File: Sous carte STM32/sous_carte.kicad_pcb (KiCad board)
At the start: 2 copper layers, 9 parts, among them J1 RJ45, P1 CONN_25X2, P2 CONN_25X2, P3 CONN_10, P4 CONN_10, P5 CONN_25X2, P6 CONN_2, P7 CONN_2, P8 CONN_2

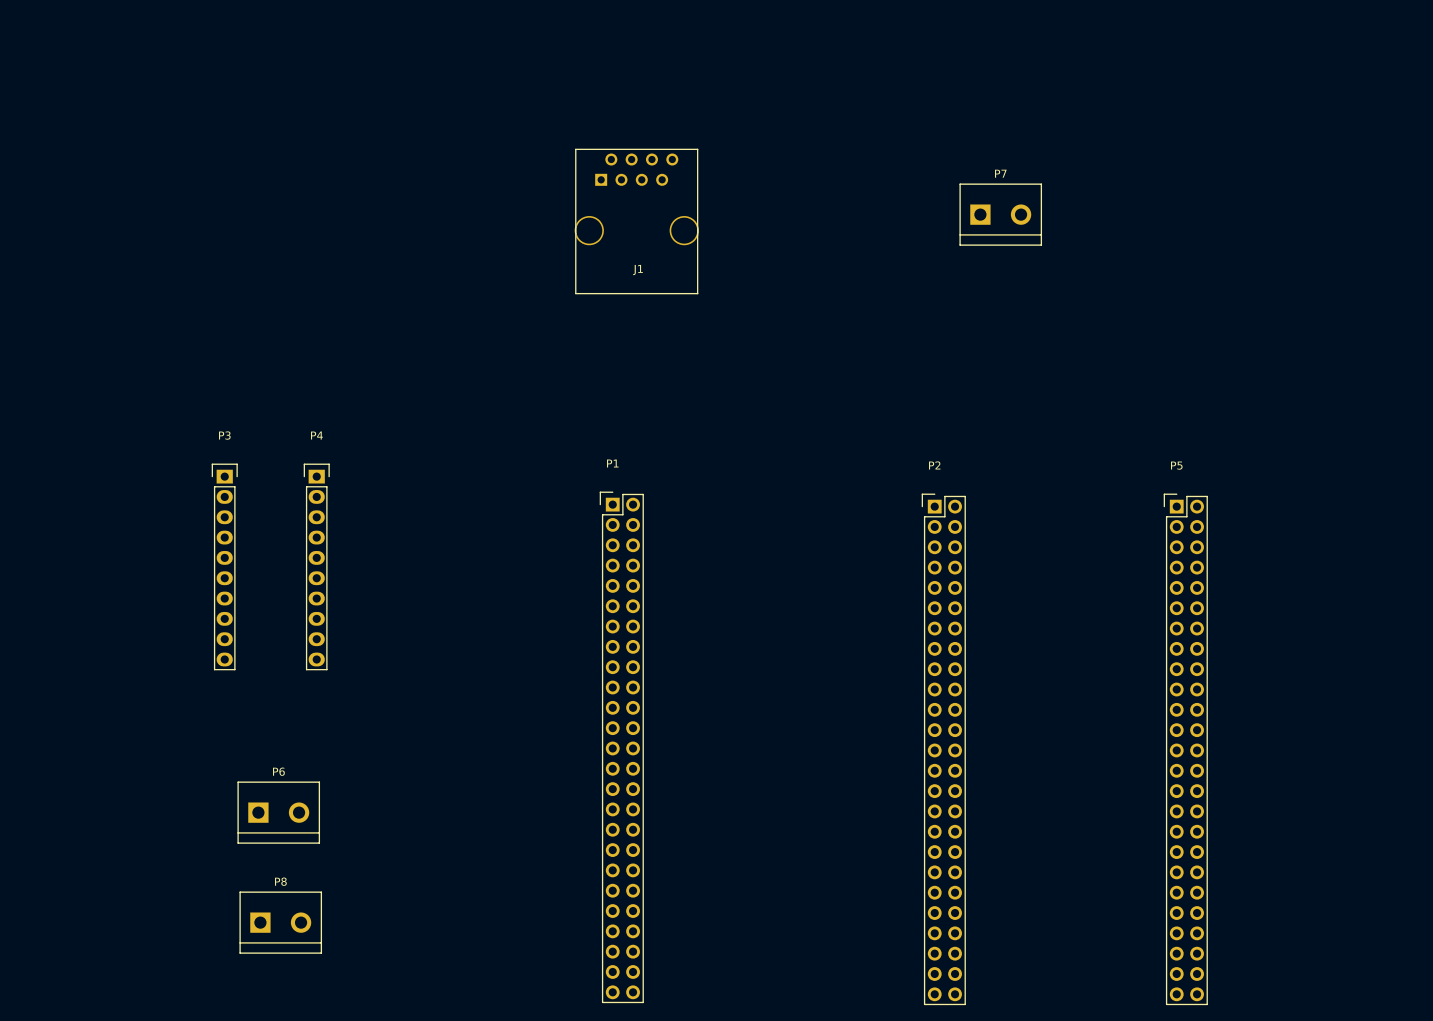
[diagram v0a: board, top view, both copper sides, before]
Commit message: fin schemas + début routage
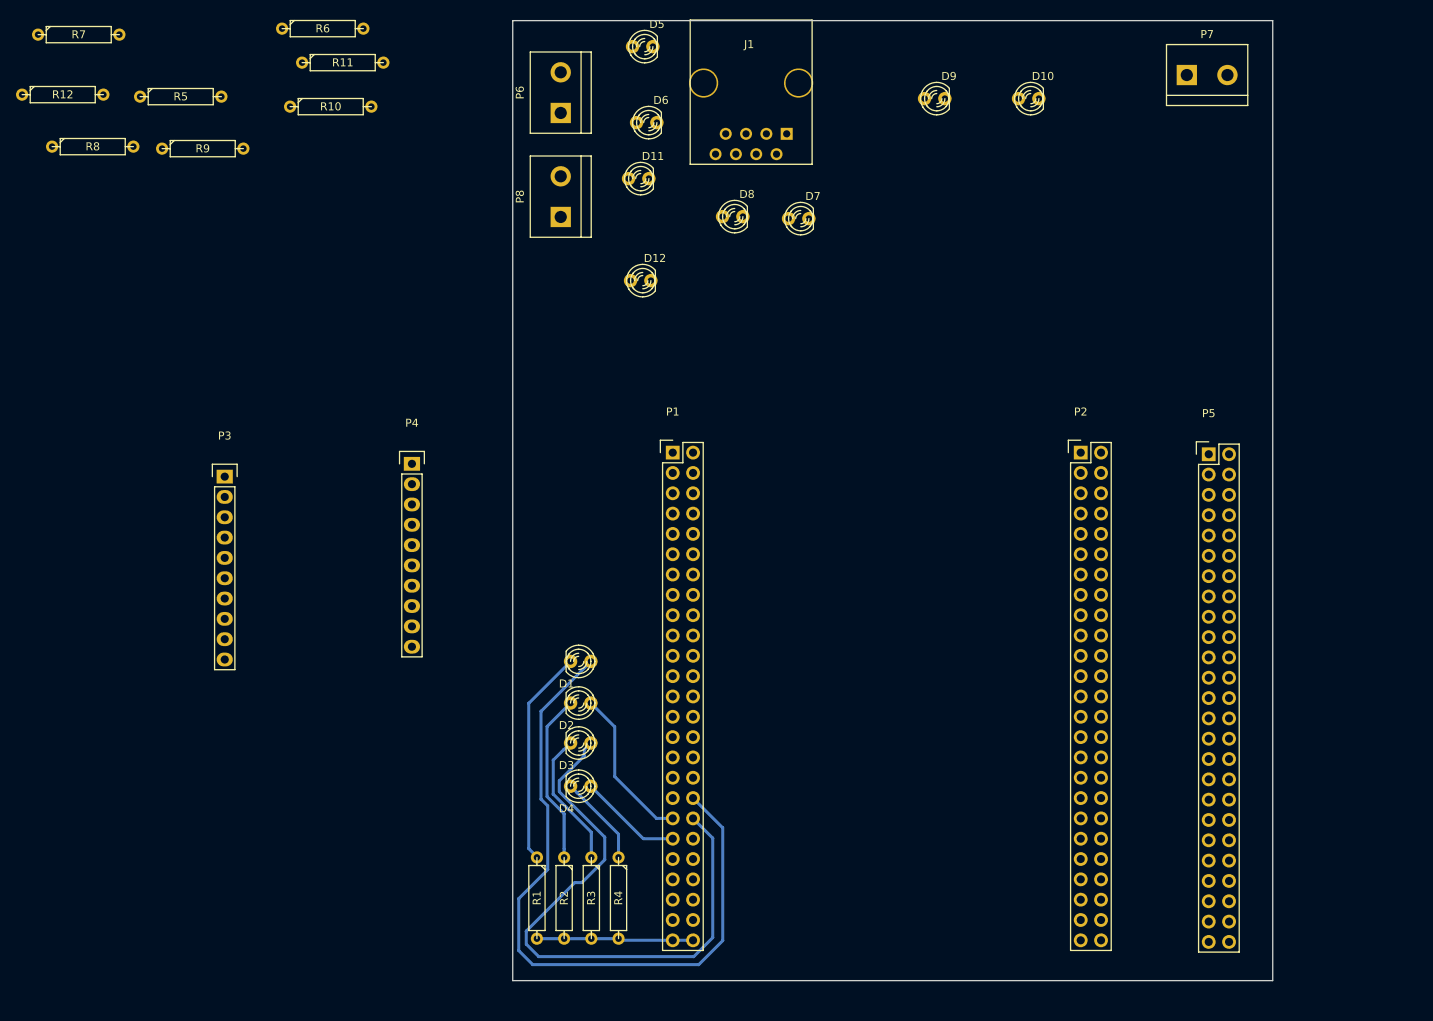
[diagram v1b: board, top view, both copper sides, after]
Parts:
- added D1: LED, LEDs:LED-3MM, F.Cu at (98.5, 126.1)
- added D10: LED, LEDs:LED-3MM, F.Cu at (154.5, 55.8)
- added D11: LED, LEDs:LED-3MM, F.Cu at (105.8, 65.8)
- added D12: LED, LEDs:LED-3MM, F.Cu at (106.0, 78.5)
- added D2: LED, LEDs:LED-3MM, F.Cu at (98.5, 131.3)
- added D3: LED, LEDs:LED-3MM, F.Cu at (98.5, 136.3)
- added D4: LED, LEDs:LED-3MM, F.Cu at (98.5, 141.7)
- added D5: LED, LEDs:LED-3MM, F.Cu at (106.2, 49.2)
- added D6: LED, LEDs:LED-3MM, F.Cu at (106.8, 58.8)
- added D7: LED, LEDs:LED-3MM, F.Cu at (125.8, 70.8)
- added D8: LED, LEDs:LED-3MM, F.Cu at (117.5, 70.5)
- added D9: LED, LEDs:LED-3MM, F.Cu at (142.8, 55.8)
- added R1: R, Discret:R4, F.Cu at (93.0, 155.7)
- added R10: R, Discret:R4, F.Cu at (67.2, 56.8)
- added R11: R, Discret:R4, F.Cu at (68.8, 51.2)
- added R12: R, Discret:R4, F.Cu at (33.8, 55.2)
- added R2: R, Discret:R4, F.Cu at (96.4, 155.7)
- added R3: R, Discret:R4, F.Cu at (99.8, 155.7)
- added R4: R, Discret:R4, F.Cu at (103.2, 155.7)
- added R5: R, Discret:R4, F.Cu at (48.5, 55.5)
- added R6: R, Discret:R4, F.Cu at (66.2, 47.0)
- added R7: R, Discret:R4, F.Cu at (35.8, 47.8)
- added R8: R, Discret:R4, F.Cu at (37.5, 61.8)
- added R9: R, Discret:R4, F.Cu at (51.2, 62.0)
- moved P8 97.3 mm to (96.0, 68.0), turned to 90 degrees
- moved P6 96.7 mm to (96.0, 55.0), turned to 90 degrees
- moved P7 31.1 mm to (176.8, 52.8)
- moved J1 23.3 mm to (119.8, 53.8), turned to 180 degrees
- moved P2 19.5 mm to (161.0, 100.0)
- moved P4 12.0 mm to (77.4, 101.4)
- moved P1 9.92 mm to (110.0, 100.0)
- moved P5 7.67 mm to (177.0, 100.2)
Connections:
- net +3.3V renamed 3V3
- net +5V renamed 5V
- net Net-(P1-Pad10) renamed C2
- net Net-(P1-Pad19) renamed C5
- net Net-(P1-Pad20) renamed C4
- net Net-(P1-Pad21) renamed B1
- net Net-(P1-Pad22) renamed B0
- net Net-(P1-Pad24) renamed B2
- net Net-(P1-Pad3) renamed VDD1
- net Net-(P1-Pad4) renamed VDD2
- net Net-(P1-Pad41) renamed D9
- net Net-(P1-Pad42) renamed D10
- net Net-(P1-Pad43) renamed D11
- net Net-(P1-Pad44) renamed D12
- net Net-(P1-Pad45) renamed D13
- net Net-(P1-Pad46) renamed D14
- net Net-(P1-Pad47) renamed D15
- net Net-(P1-Pad48) renamed NC
- net Net-(P1-Pad6) renamed NRST
- net Net-(P1-Pad7) renamed C1
- net Net-(P1-Pad8) renamed C0
- net Net-(P1-Pad9) renamed C3
- net Net-(P2-Pad10) renamed C15
- net Net-(P2-Pad12) renamed C13
- net Net-(P2-Pad15) renamed E2
- net Net-(P2-Pad16) renamed E3
- net Net-(P2-Pad17) renamed E0
- net Net-(P2-Pad18) renamed E1
- net Net-(P2-Pad21) renamed BOOT0
- net Net-(P2-Pad22) renamed VDD3
- net Net-(P2-Pad27) renamed D7
- net Net-(P2-Pad31) renamed D3
- net Net-(P2-Pad32) renamed D4
- net Net-(P2-Pad33) renamed D1
- net Net-(P2-Pad39) renamed A14
- net Net-(P2-Pad40) renamed A15
- net Net-(P2-Pad42) renamed A13
- net Net-(P2-Pad7) renamed H0
- net Net-(P2-Pad8) renamed H1
- net Net-(P2-Pad9) renamed C14
- P1 pad 11: UART4_RX -> A1
- P1 pad 12: UART4_TX -> A0
- P1 pad 13: UART2_RX -> A3
- P1 pad 14: UART2_TX -> A2
- P1 pad 15: Net-(P1-Pad15) -> A5
- P1 pad 16: Net-(P1-Pad16) -> A4
- P1 pad 17: Net-(P1-Pad17) -> A7
- P1 pad 18: Net-(P1-Pad18) -> A6
- P1 pad 25: Net-(P1-Pad25) -> E7
- P1 pad 26: Net-(P1-Pad26) -> E8
- P1 pad 27: Net-(P1-Pad27) -> E9
- P1 pad 28: Net-(P1-Pad28) -> E10
- P1 pad 29: Net-(P1-Pad29) -> E11
- P1 pad 30: Net-(P1-Pad30) -> E12
- P1 pad 31: Net-(P1-Pad31) -> E13
- P1 pad 32: Net-(P1-Pad32) -> E14
- P1 pad 33: Net-(P1-Pad33) -> E15
- P1 pad 34: Net-(P1-Pad34) -> B10
- P1 pad 35: Net-(P1-Pad35) -> B11
- P1 pad 36: Net-(P1-Pad36) -> B12
- P1 pad 37: Net-(P1-Pad37) -> B13
- P1 pad 38: Net-(P1-Pad38) -> B14
- P1 pad 39: Net-(P1-Pad39) -> B15
- P2 pad 11: Net-(P2-Pad11) -> E6
- P2 pad 13: Net-(P2-Pad13) -> E4
- P2 pad 14: Net-(P2-Pad14) -> E5
- P2 pad 19: Net-(P2-Pad19) -> B8
- P2 pad 20: Net-(P2-Pad20) -> B9
- P2 pad 23: Net-(P2-Pad23) -> B6
- P2 pad 24: Net-(P2-Pad24) -> B7
- P2 pad 25: Net-(P2-Pad25) -> B4
- P2 pad 26: Net-(P2-Pad26) -> B5
- P2 pad 28: Net-(P2-Pad28) -> B3
- P2 pad 29: Net-(P2-Pad29) -> UART2_TX
- P2 pad 30: Net-(P2-Pad30) -> D6
- P2 pad 34: Net-(P2-Pad34) -> D2
- P2 pad 35: Net-(P2-Pad35) -> C12
- P2 pad 36: Net-(P2-Pad36) -> C12
- P2 pad 37: Net-(P2-Pad37) -> C10
- P2 pad 38: Net-(P2-Pad38) -> UART4_RX
- P2 pad 41: Net-(P2-Pad41) -> A10
- P2 pad 43: Net-(P2-Pad43) -> A8
- P2 pad 44: Net-(P2-Pad44) -> A9
- P2 pad 45: Net-(P2-Pad45) -> C8
- P2 pad 46: Net-(P2-Pad46) -> C9
- P2 pad 47: UART6_TX -> C6
- P2 pad 48: UART6_RX -> C7
- P3 pad 2: UART2_RX -> UART4_RX
- P3 pad 3: UART2_TX -> C10
- P5 pad 11: Net-(P1-Pad16) -> A0
- P5 pad 13: Net-(P1-Pad17) -> A3
- P5 pad 14: Net-(P5-Pad14) -> E4
- P5 pad 15: Net-(P1-Pad18) -> A2
- P5 pad 16: Net-(P5-Pad16) -> E5
- P5 pad 18: Net-(P5-Pad18) -> E6
- P5 pad 20: Net-(P5-Pad20) -> E7
- P5 pad 22: Net-(P5-Pad22) -> E8
- P5 pad 24: Net-(P5-Pad24) -> E9
- P5 pad 26: Net-(P5-Pad26) -> E10
- P5 pad 27: Net-(P5-Pad27) -> B10
- P5 pad 28: Net-(P5-Pad28) -> E11
- P5 pad 29: Net-(P5-Pad29) -> B11
- P5 pad 30: Net-(P5-Pad30) -> E12
- P5 pad 31: Net-(P5-Pad31) -> B8
- P5 pad 32: Net-(P5-Pad32) -> E13
- P5 pad 33: Net-(P5-Pad33) -> B9
- P5 pad 34: Net-(P5-Pad34) -> E14
- P5 pad 35: Net-(P5-Pad35) -> B6
- P5 pad 36: Net-(P5-Pad36) -> E15
- P5 pad 37: Net-(P5-Pad37) -> B7
- P5 pad 39: Net-(P5-Pad39) -> B4
- P5 pad 41: Net-(P5-Pad41) -> B5
- P5 pad 43: Net-(P5-Pad43) -> B3
- P5 pad 45: Net-(P2-Pad41) -> C8
- P5 pad 47: Net-(P2-Pad43) -> C9
- P5 pad 49: Net-(P2-Pad44) -> GND
- P5 pad 9: Net-(P1-Pad15) -> A1
- P6 pad 1: UART4_RX -> D6
- P6 pad 2: UART4_TX -> UART2_TX
- P8 pad 1: UART6_RX -> D2
- P8 pad 2: UART6_TX -> C12
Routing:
- net B12: track 0.00 -> 87.4 mm
- net B14: track 0.00 -> 74.6 mm
- net Net-(D1-Pad2): track 0.00 -> 27.1 mm
- net Net-(D2-Pad2): track 0.00 -> 21.4 mm
- net B13: track 0.00 -> 19.8 mm
- net GND: track 0.00 -> 19.6 mm
- net Net-(D3-Pad2): track 0.00 -> 17.2 mm
- net B15: track 0.00 -> 12.9 mm
- net Net-(D4-Pad2): track 0.00 -> 11.4 mm
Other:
- board outline added: 95 x 120 mm
- net class Default: clearance 0.2 -> 0.381; trace_width 0.25 -> 0.381
- rule trace_clearance: 0.2 -> 0.381

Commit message: routage
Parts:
- added D13: LED, LEDs:LED-3MM, F.Cu at (161.5, 51.2)
- added R13: R, Discret:R4, F.Cu at (161.8, 59.8)
- moved R9 110.6 mm to (160.8, 77.2), turned to 180 degrees
- moved R7 104.5 mm to (137.0, 73.5), turned to 180 degrees
- moved R8 100.7 mm to (137.0, 77.2), turned to 180 degrees
- moved R10 96.5 mm to (160.8, 80.8), turned to 180 degrees
- moved R12 90.5 mm to (119.5, 84.2)
- moved P3 90.4 mm to (144.0, 111.8)
- moved R5 73.2 mm to (119.5, 73.5)
- moved R6 61.2 mm to (119.5, 77.2)
- moved R11 58.7 mm to (119.5, 80.8)
- moved P4 55.6 mm to (132.0, 111.8)
- moved D9 41.5 mm to (179.8, 74.5)
- moved D10 35.5 mm to (179.8, 80.8)
- moved D8 25.0 mm to (133.5, 51.2)
- moved P8 15.5 mm to (96.0, 83.5)
- moved D7 15.4 mm to (133.5, 57.5)
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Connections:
- net C10 renamed UART4_TX
- net D2 renamed UART5_RX
- net UART3_TX renamed D8
- D11 pad 1: C12 -> UART5_TX
- D8 pad 1: UART3_RX -> D9
- J1 pad 3: UART3_RX -> D9
- P2 pad 35: C12 -> UART5_TX
- P2 pad 36: C12 -> D0
- P5 pad 10: Net-(P5-Pad10) -> GND
- P5 pad 4: Net-(P5-Pad4) -> GND
- P5 pad 40: Net-(P5-Pad40) -> GND
- P5 pad 42: Net-(P5-Pad42) -> GND
- P5 pad 44: Net-(P5-Pad44) -> GND
- P5 pad 46: Net-(P5-Pad46) -> GND
- P5 pad 48: Net-(P5-Pad48) -> GND
- P5 pad 6: Net-(P5-Pad6) -> GND
- P5 pad 8: Net-(P5-Pad8) -> GND
- P8 pad 2: C12 -> UART5_TX
- R10 pad 2: Net-(R10-Pad2) -> GND
- R11 pad 2: Net-(R11-Pad2) -> GND
- R6 pad 2: Net-(R6-Pad2) -> GND
- R7 pad 2: Net-(R7-Pad2) -> GND
- R8 pad 2: Net-(R8-Pad2) -> GND
- R9 pad 2: Net-(R9-Pad2) -> GND
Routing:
- net GND: track 19.6 -> 373.7 mm
- net D6: track 0.00 -> 190.9 mm, vias 0 -> 2
- net UART5_RX: track 0.00 -> 163.9 mm, vias 0 -> 2
- net D9: track 0.00 -> 151.3 mm, vias 0 -> 2
- net UART2_TX: track 0.00 -> 148.5 mm, vias 0 -> 2
- net UART5_TX: track 0.00 -> 139.2 mm, vias 0 -> 2
- net D8: track 0.00 -> 105.7 mm, vias 0 -> 2
- net 5V: track 0.00 -> 85.5 mm
- net UART4_TX: track 0.00 -> 64.9 mm, vias 0 -> 1
- net UART4_RX: track 0.00 -> 54.2 mm, vias 0 -> 1
- net Net-(D11-Pad2): track 0.00 -> 40.3 mm
- net Net-(D5-Pad2): track 0.00 -> 38.7 mm
- net Net-(D8-Pad2): track 0.00 -> 36.9 mm
- net C8: track 0.00 -> 33.6 mm, vias 0 -> 2
- net B5: track 0.00 -> 30.6 mm
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
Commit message: essayé d'avancer
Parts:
- P3, P4, P5: moved to B.Cu
- moved P5 79.3 mm to (97.7, 98.1), turned to 180 degrees
- moved P4 50.2 mm to (180.1, 97.6), turned to 90 degrees
- moved P3 44.6 mm to (180.1, 85.6), turned to 90 degrees
- moved D4 40.0 mm to (138.2, 146.9), turned to 270 degrees
- moved D3 36.2 mm to (133.1, 146.9), turned to 270 degrees
- moved R4 35.0 mm to (138.2, 156.5)
- moved P1 33.8 mm to (143.8, 98.1)
- moved P2 33.8 mm to (194.8, 98.1)
- moved D2 33.4 mm to (128.0, 146.9), turned to 270 degrees
- moved R3 33.3 mm to (133.1, 156.5)
- moved D1 32.1 mm to (122.9, 146.9), turned to 270 degrees
- moved R2 31.6 mm to (128.0, 156.5)
- moved R1 29.9 mm to (122.9, 156.5)
- moved R9 28.6 mm to (173.4, 51.6), turned to 0 degrees
- moved D9 27.6 mm to (164.5, 51.6)
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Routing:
- net UART5_RX: track 163.9 -> 12.9 mm, vias 2 -> 0
- net D6: track 190.9 -> 51.8 mm, vias 2 -> 0
- net GND: track 373.7 -> 271.1 mm
- net D9: track 151.3 -> 57.3 mm, vias 2 -> 0
- net C9: track 14.6 -> 85.0 mm
- net D8: track 105.7 -> 37.6 mm, vias 2 -> 0
- net C1: track 0.00 -> 49.4 mm
- net C3: track 0.00 -> 49.4 mm
- net B11: track 0.00 -> 49.2 mm
- net C5: track 0.00 -> 47.1 mm
- net A1: track 0.00 -> 47.1 mm
- net B1: track 0.00 -> 46.1 mm
- net A3: track 0.00 -> 46.1 mm
- net UART4_TX: track 64.9 -> 107.8 mm, vias 1 -> 0
- net C8: track 33.6 -> 0.00 mm, vias 2 -> 0
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- added copper zone on B.Cu, net GND
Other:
- board size 95 x 120 mm -> 113 x 120.1 mm

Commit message: on avance
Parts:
- removed P4: CONN_10, Pin_Headers:Pin_Header_Straight_1x10
- P3: value CONN_10 -> CONN_4; moved to F.Cu
- moved P3 41.9 mm to (155.4, 51.8), turned to 0 degrees
- moved D9 7.50 mm to (164.4, 59.1)
- moved R9 7.50 mm to (173.3, 59.1)
- moved D10 7.00 mm to (164.4, 51.5)
- moved R10 7.00 mm to (173.3, 51.5)
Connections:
- net D6 renamed UART2_RX
- net D8 renamed UART3_TX
- net UART5_RX renamed D2
- net UART5_TX renamed C12
- P3 pad 1: 3V3 -> GND
- P3 pad 10: GND -> (no net)
- P3 pad 2: UART4_RX -> 5V
- P3 pad 3: UART4_TX -> UART4_RX
- P3 pad 4: Net-(P3-Pad4) -> UART4_TX
- P3 pad 5: 3V3 -> (no net)
- P3 pad 6: Net-(P3-Pad6) -> (no net)
- P3 pad 7: Net-(P3-Pad7) -> (no net)
- P3 pad 8: Net-(P3-Pad8) -> (no net)
- P3 pad 9: Net-(P3-Pad9) -> (no net)
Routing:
- net D2: track 12.9 -> 227.7 mm
- net UART2_RX: track 51.8 -> 182.1 mm, vias 0 -> 2
- net C12: track 138.0 -> 17.5 mm
- net UART2_TX: track 157.1 -> 39.9 mm
- net UART4_RX: track 46.3 -> 129.0 mm, vias 0 -> 2
- net D9: track 57.3 -> 130.5 mm, vias 0 -> 2
- net 3V3: track 38.6 -> 2.54 mm
- net 5V: track 64.0 -> 95.1 mm, vias 0 -> 2
- net C9: track 85.0 -> 114.4 mm, vias 0 -> 2
- net GND: track 271.1 -> 291.5 mm, vias 0 -> 2
- net UART4_TX: track 107.8 -> 106.8 mm
